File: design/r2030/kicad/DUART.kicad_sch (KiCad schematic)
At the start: 17 parts, among them IC4 XR68C681CJTR-F, J1 UART_A, J2 UART_B, J4 Conn_01x06, J7 Conn_01x01_Male, Q1 3.6864MHz

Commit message: Update to Kicad 7
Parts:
- J1, J2: symbol Connector:Conn_01x06_Male -> Connector:Conn_01x06_Pin
- J7: symbol Connector:Conn_01x01_Male -> Connector:Conn_01x01_Pin

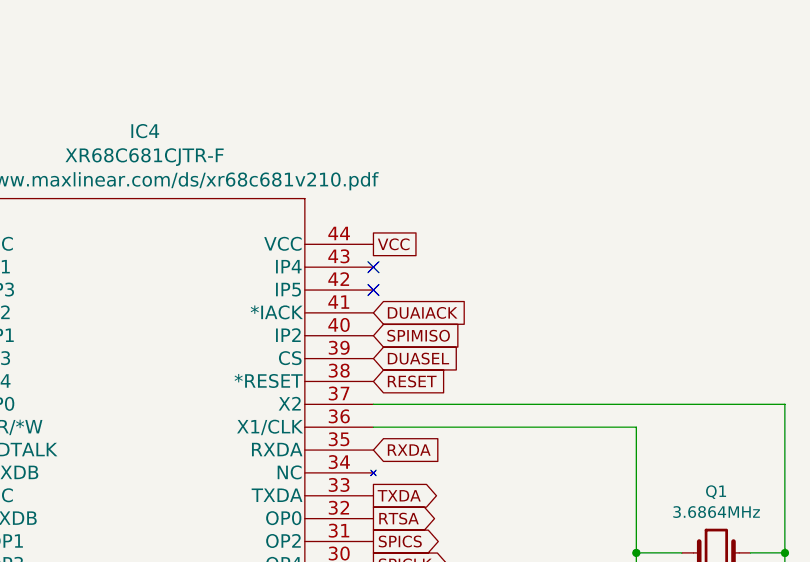
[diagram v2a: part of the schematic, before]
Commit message: Swap TX/RX & CTS/RTS silkscreen r2030
  * Swap over labels
  * Add arrows
  * Some board tidy up
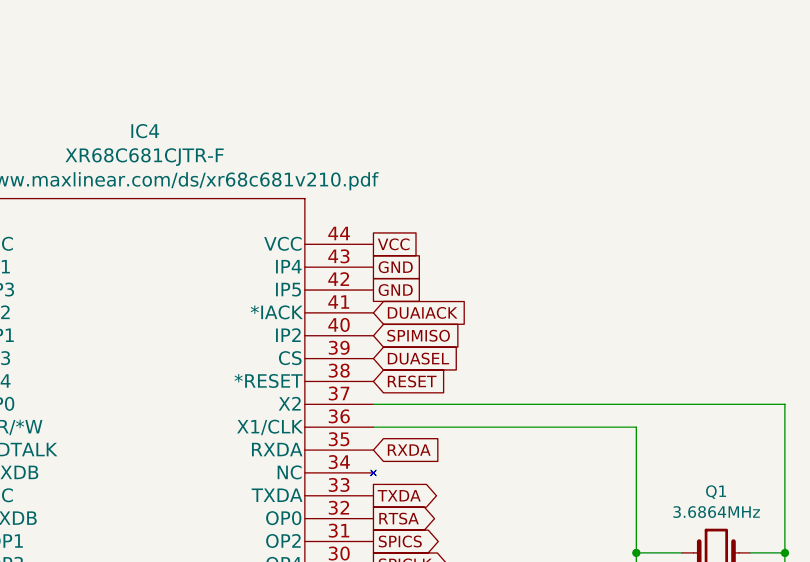
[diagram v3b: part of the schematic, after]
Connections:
- net GND: now also IC4.42 (IP5), IC4.43 (IP4)
- no-connect marks 2 -> 0
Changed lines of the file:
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@@
   (title_block
     (title "ROSCO_M68K CLASSIC MC68030 EDITION")
-    (date "2023-12-05")
+    (date "2023-12-10")
     (rev "2.0")
     (company "The Really Old-School Company Limited")
@@
   (junction (at 191.77 80.01) (diameter 0) (color 0 0 0 0)
   )
-  (no_connect (at 162.56 50.8))
-  (no_connect (at 162.56 48.26))
   (wire (pts (xy 92.71 52.07) (xy 86.36 52.07))
     (stroke (width 0) (type default))
@@
     )
   )
+  (global_label "GND" (shape passive) (at 162.56 48.26 0) (fields_autoplaced)
+    (effects (font (size 1.27 1.27)) (justify left))
+    (property "Intersheetrefs" "${INTERSHEET_REFS}" (at 167.809 48.26 0)
+      (effects (font (size 1.27 1.27)) (justify left) hide)
+    )
+  )
   (global_label "SPICLK" (shape input) (at 95.25 158.75 180) (fields_autoplaced)
     (effects (font (size 1.27 1.27)) (justify right))
@@
     )
   )
+  (global_label "GND" (shape passive) (at 162.56 50.8 0) (fields_autoplaced)
+    (effects (font (size 1.27 1.27)) (justify left))
+    (property "Intersheetrefs" "${INTERSHEET_REFS}" (at 167.809 50.8 0)
+      (effects (font (size 1.27 1.27)) (justify left) hide)
+    )
+  )
